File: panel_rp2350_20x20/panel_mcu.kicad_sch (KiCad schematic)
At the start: 32 parts, among them SW1 SW_Push, SW2 SW_Push, U1 APS6404L-3SQR, U2 RP2354B_80QFN, Y1 ABM8-272-T3

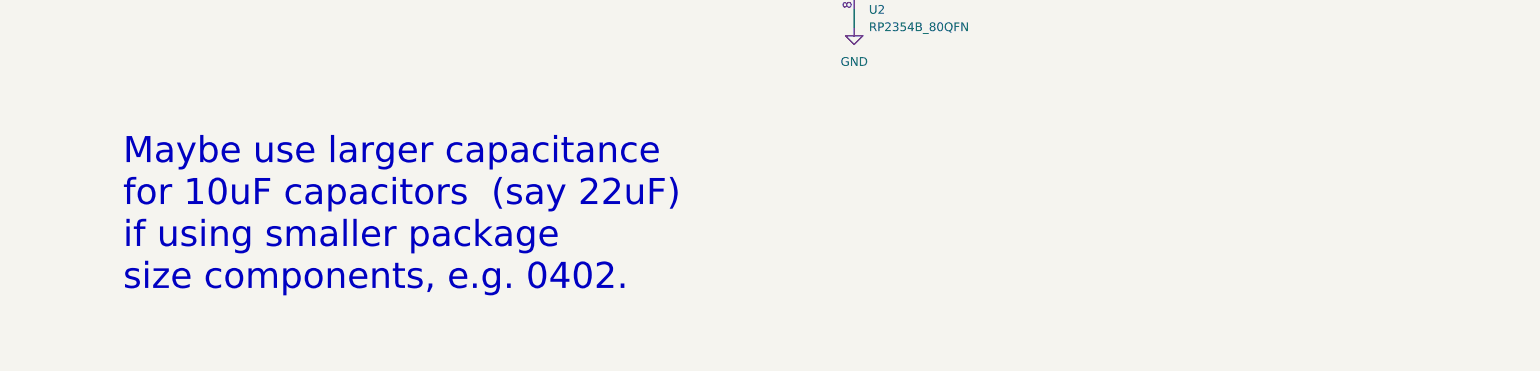
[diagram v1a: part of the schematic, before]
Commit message: Worked on rp2350 20x20 panel layout and routing.
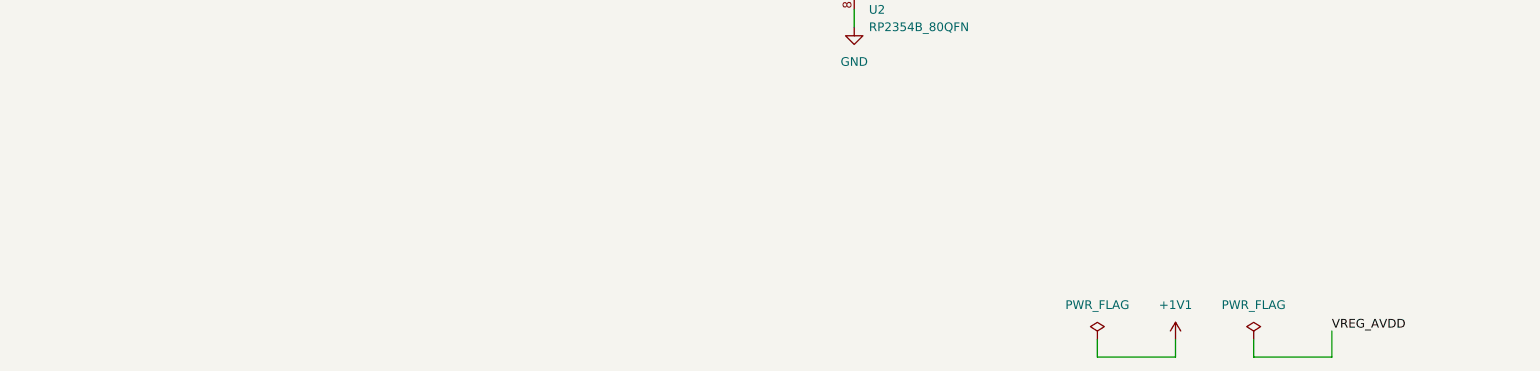
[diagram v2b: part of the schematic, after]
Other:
- note removed: "Maybe use larger capacitance for 10uF capacitors (say 22uF) if using smaller package size components, e.g. 0402."

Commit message: Worked on setup for fabrication.
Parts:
- R6: LCSC Part # (none) -> C295794
- R7, R8: LCSC Part # (none) -> C473051
- SW1, SW2: LCSC Part # (none) -> C720477
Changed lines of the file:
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@@
+			)
+		)
+		(property "LCSC Part #" "C473051"
+			(at 256.54 66.04 0)
+			(effects
+				(font
+					(size 1.27 1.27)
+				)
 			)
 		)
@@
 			)
 		)
+		(property "LCSC Part #" "C720477"
+			(at 63.5 207.01 0)
+			(effects
+				(font
+					(size 1.27 1.27)
+				)
+			)
+		)
 		(pin "1"
 		)
@@
 			)
 		)
+		(property "LCSC Part #" "C295794"
+			(at 148.59 60.96 0)
+			(effects
+				(font
+					(size 1.27 1.27)
+				)
+			)
+		)
 		(pin "1"
 		)
@@
 			)
 		)
+		(property "LCSC Part #" "C720477"
+			(at 44.45 178.435 0)
+			(effects
+				(font
+					(size 1.27 1.27)
+				)
+			)
+		)
 		(pin "1"
 		)
@@
 			(at 256.54 74.93 0)
 			(effects
+				(font
+					(size 1.27 1.27)
+				)
+			)
+		)
+		(property "LCSC Part #" "C473051"
+			(at 256.54 74.93 0)
+			(effects

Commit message: Worked on fab files.
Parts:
- C1, C2: LCSC Part # (none) -> C541259
- C10, C11, C12, C13, C14, C15, C16, C17, C18, C3, C6, C9: LCSC Part # (none) -> C76939
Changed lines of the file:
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@@
+			)
+		)
+		(property "LCSC Part #" "C541259"
+			(at 48.26 116.84 0)
+			(effects
+				(font
+					(size 1.27 1.27)
+				)
+				(hide yes)
 			)
 		)
@@
 			)
 		)
+		(property "LCSC Part #" "C541259"
+			(at 48.26 127 0)
+			(effects
+				(font
+					(size 1.27 1.27)
+				)
+				(hide yes)
+			)
+		)
 		(pin "1"
 		)
@@
 			)
 		)
+		(property "LCSC Part #" "C76939"
+			(at 257.81 36.83 0)
+			(effects
+				(font
+					(size 1.27 1.27)
+				)
+			)
+		)
 		(pin "1"
 		)
@@
 			)
 		)
+		(property "LCSC Part #" "C76939"
+			(at 269.24 36.83 0)
+			(effects
+				(font
+					(size 1.27 1.27)
+				)
+			)
+		)
 		(pin "1"
 		)
@@
 			)
 		)
+		(property "LCSC Part #" "C76939"
+			(at 280.67 36.83 0)
+			(effects
+				(font
+					(size 1.27 1.27)
+				)
+			)
+		)
 		(pin "1"
 		)
@@
 			)
 		)
+		(property "LCSC Part #" "C76939"
+			(at 292.1 36.83 0)
+			(effects
+				(font
+					(size 1.27 1.27)
+				)
+			)
+		)
 		(pin "1"
 		)
@@
 			)
 		)
+		(property "LCSC Part #" "C76939"
+			(at 303.53 36.83 0)
+			(effects
+				(font
+					(size 1.27 1.27)
+				)
+			)
+		)
 		(pin "1"
 		)
@@
 			)
 		)
+		(property "LCSC Part #" "C76939"
+			(at 314.96 36.83 0)
+			(effects
+				(font
+					(size 1.27 1.27)
+				)
+			)
+		)
 		(pin "1"
 		)
@@
 		)
 		(property "Description" ""
+			(at 172.72 36.83 0)
+			(effects
+				(font
+					(size 1.27 1.27)
+				)
+			)
+		)
+		(property "LCSC Part #" "C76939"
 			(at 172.72 36.83 0)
 			(effects
@@
 					(size 1.27 1.27)
 				)
+				(hide yes)
 			)
 		)
@@
 			)
 		)
+		(property "LCSC Part #" "C76939"
+			(at 246.38 36.83 0)
+			(effects
+				(font
+					(size 1.27 1.27)
+				)
+			)
+		)
 		(pin "1"
 		)
@@
 		)
 		(property "Description" ""
+			(at 326.39 36.83 0)
+			(effects
+				(font
+					(size 1.27 1.27)
+				)
+			)
+		)
+		(property "LCSC Part #" "C76939"
 			(at 326.39 36.83 0)
 			(effects
@@
 					(size 1.27 1.27)
 				)
+				(hide yes)
 			)
 		)
@@
 			)
 		)
+		(property "LCSC Part #" "C76939"
+			(at 149.86 36.83 0)
+			(effects
+				(font
+					(size 1.27 1.27)
+				)
+			)
+		)
 		(pin "1"
 		)
@@
 			)
 		)
+		(property "LCSC Part #" "C76939"
+			(at 88.9 76.2 0)
+			(effects
+				(font
+					(size 1.27 1.27)
+				)
+			)
+		)
 		(pin "1"
 		)
@@
 			)
 		)
+		(property "LCSC Part #" "C76939"
+			(at 234.95 36.83 0)
+			(effects
+				(font
+					(size 1.27 1.27)
+				)
+			)
+		)
 		(pin "1"
 		)
@@
 					(size 1.27 1.27)
 				)
+				(hide yes)
 			)
 		)
@@
 					(size 1.27 1.27)
 				)
+				(hide yes)
 			)
 		)
@@
 					(size 1.27 1.27)
 				)
-			)
-		)
+				(hide yes)
+			)
+		)

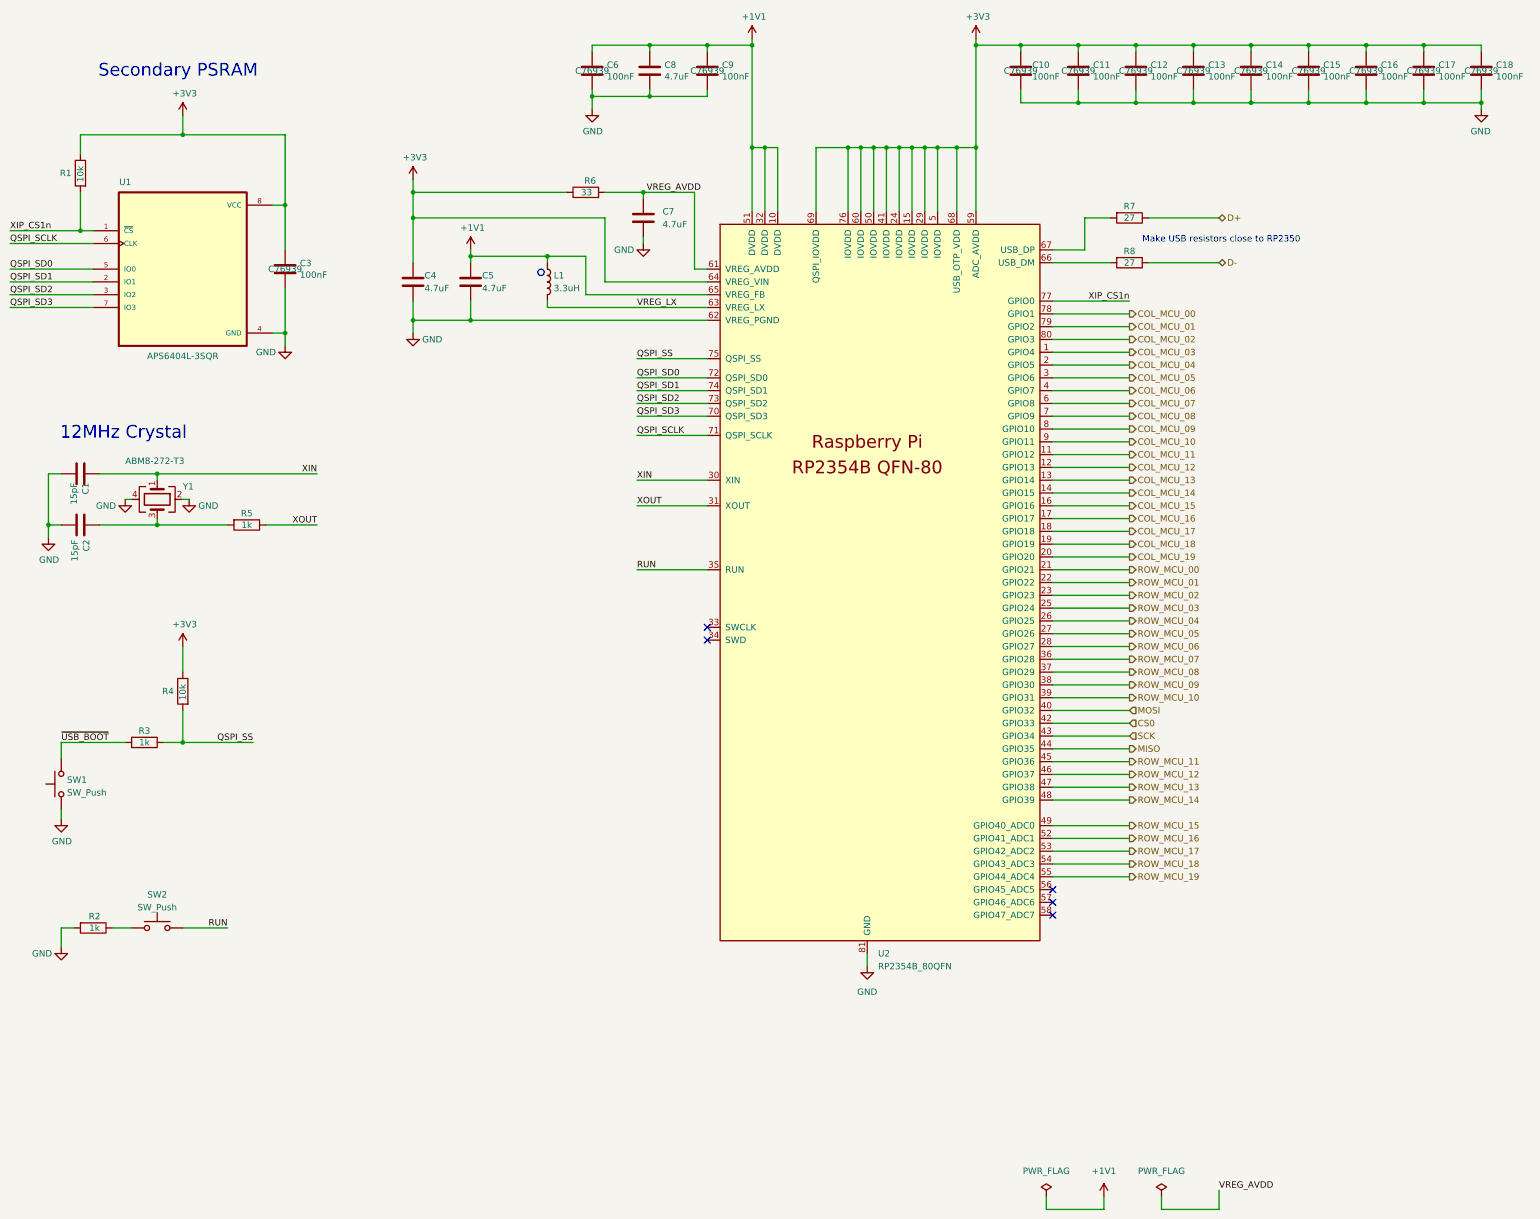
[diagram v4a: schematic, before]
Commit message: Worked on routing and fabrication setup.
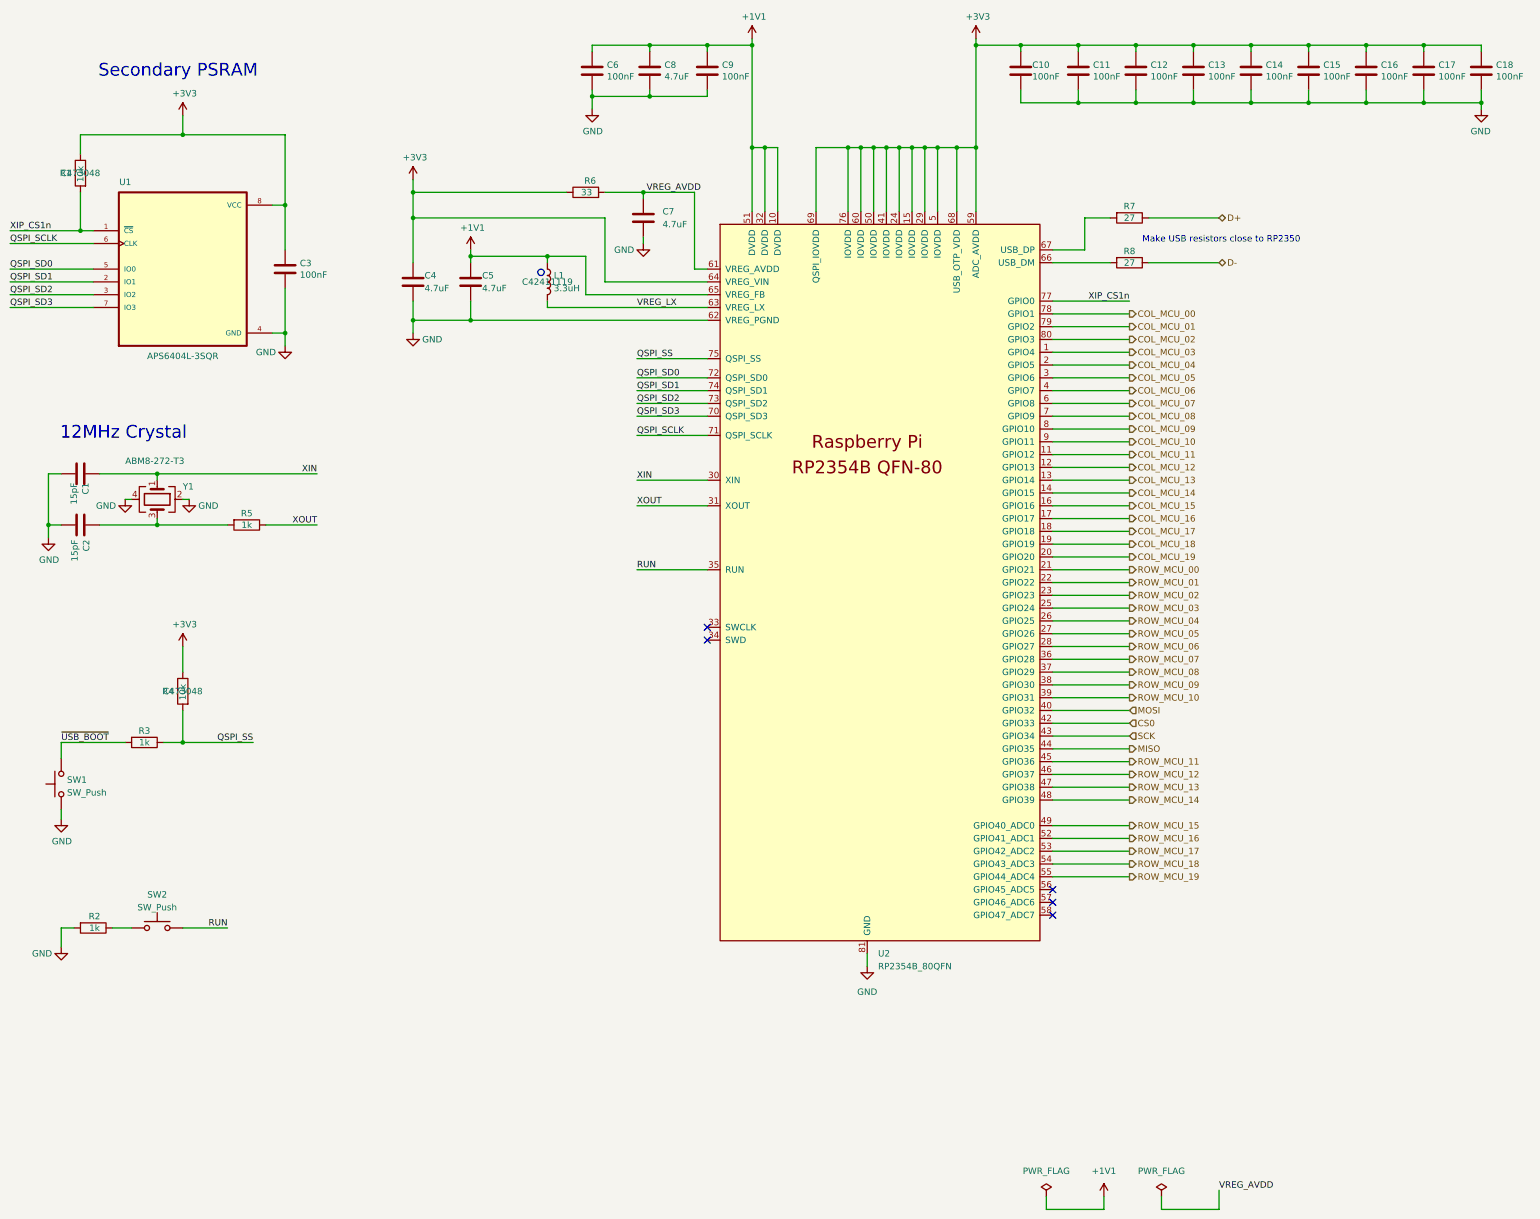
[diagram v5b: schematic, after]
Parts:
- C4, C5, C7, C8: LCSC Part # (none) -> C368809
- L1: LCSC Part # (none) -> C42411119
- R1, R4: LCSC Part # (none) -> C473048
- R2, R3, R5: LCSC Part # (none) -> C270365
- U1: LCSC Part # (none) -> C3040877
- U2: LCSC Part # (none) -> C39843328
- Y1: LCSC Part # (none) -> C20625731
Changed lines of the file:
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@@
 					(size 1.27 1.27)
 				)
+				(hide yes)
 			)
 		)
@@
 					(size 1.27 1.27)
 				)
+				(hide yes)
 			)
 		)
@@
 					(size 1.27 1.27)
 				)
+				(hide yes)
 			)
 		)
@@
 					(size 1.27 1.27)
 				)
+				(hide yes)
 			)
 		)
@@
 					(size 1.27 1.27)
 				)
+				(hide yes)
 			)
 		)
@@
 					(size 1.27 1.27)
 				)
+				(hide yes)
 			)
 		)
@@
 					(size 1.27 1.27)
 				)
+				(hide yes)
 			)
 		)
@@
 					(size 1.27 1.27)
 				)
+				(hide yes)
 			)
 		)
@@
 					(size 1.27 1.27)
 				)
+				(hide yes)
 			)
 		)
@@
 					(size 1.27 1.27)
 				)
+				(hide yes)
 			)
 		)
@@
 					(size 1.27 1.27)
 				)
+				(hide yes)
 			)
 		)
@@
 					(size 1.27 1.27)
 				)
+				(hide yes)
 			)
 		)
@@
 					(size 1.27 1.27)
 				)
+				(hide yes)
 			)
 		)
@@
 					(size 1.27 1.27)
 				)
+				(hide yes)
 			)
 		)
@@
 					(size 1.27 1.27)
 				)
+				(hide yes)
+			)
+		)
+		(property "LCSC Part #" "C20625731"
+			(at 63.5 121.92 0)
+			(effects
+				(font
+					(size 1.27 1.27)
+				)
+				(hide yes)
 			)
 		)
@@
 			)
 		)
+		(property "LCSC Part #" "C3040877"
+			(at 68.58 76.2 0)
+			(effects
+				(font
+					(size 1.27 1.27)
+				)
+				(hide yes)
+			)
+		)
 		(pin "5"
 		)
@@
 					(size 1.27 1.27)
 				)
+				(hide yes)
 			)
 		)
@@
 					(size 1.27 1.27)
 				)
+				(hide yes)
 			)
 		)
@@
 					(size 1.27 1.27)
 				)
+				(hide yes)
 			)
 		)
@@
 					(size 1.27 1.27)
 				)
+				(hide yes)
 			)
 		)
@@
 					(size 1.27 1.27)
 				)
+				(hide yes)
 			)
 		)
@@
 					(size 1.27 1.27)
 				)
+				(hide yes)
 			)
 		)
@@
 					(size 1.27 1.27)
 				)
+				(hide yes)
 			)
 		)
@@
 					(size 1.27 1.27)
 				)
+				(hide yes)
+			)
+		)
+		(property "LCSC Part #" "C473048"
+			(at 68.58 160.02 0)
+			(effects
+				(font
+					(size 1.27 1.27)
+				)
 			)
 		)
@@
 					(size 1.27 1.27)
 				)
+				(hide yes)
+			)
+		)
+		(property "LCSC Part #" "C368809"
+			(at 160.02 66.04 0)
+			(effects
+				(font
+					(size 1.27 1.27)
+				)
+				(hide yes)
 			)
 		)
@@
 			)
 		)
+		(property "LCSC Part #" "C39843328"
+			(at 204.47 115.57 0)
+			(effects
+				(font
+					(size 1.27 1.27)
+				)
+				(hide yes)
+			)
+		)
 		(pin "64"
 		)
@@
 					(size 1.27 1.27)
 				)
+				(hide yes)
+			)
+		)
+		(property "LCSC Part #" "C270365"
+			(at 60.96 170.18 0)
+			(effects
+				(font
+					(size 1.27 1.27)
+				)
+				(hide yes)
 			)
 		)
@@
 			)
 		)
+		(property "LCSC Part #" "C42411119"
+			(at 140.97 78.74 0)
+			(effects
+				(font
+					(size 1.27 1.27)
+				)
+			)
+		)
 		(pin "1"
 		)
@@
 					(size 1.27 1.27)
 				)
+				(hide yes)
+			)
+		)
+		(property "LCSC Part #" "C368809"
+			(at 125.73 78.74 0)
+			(effects
+				(font
+					(size 1.27 1.27)
+				)
+				(hide yes)
 			)
 		)
@@
 					(size 1.27 1.27)
 				)
+				(hide yes)
+			)
+		)
+		(property "LCSC Part #" "C270365"
+			(at 81.28 127 0)
+			(effects
+				(font
+					(size 1.27 1.27)
+				)
+				(hide yes)
 			)
 		)
@@
 					(size 1.27 1.27)
 				)
+				(hide yes)
 			)
 		)
@@
 					(size 1.27 1.27)
 				)
+				(hide yes)
 			)
 		)
@@
 					(size 1.27 1.27)
 				)
+				(hide yes)
 			)
 		)
@@
 					(size 1.27 1.27)
 				)
+				(hide yes)
 			)
 		)
@@
 					(size 1.27 1.27)
 				)
+				(hide yes)
+			)
+		)
+		(property "LCSC Part #" "C368809"
+			(at 161.29 36.83 0)
+			(effects
+				(font
+					(size 1.27 1.27)
+				)
+				(hide yes)
 			)
 		)
@@
 					(size 1.27 1.27)
 				)
+				(hide yes)
 			)
 		)
@@
 					(size 1.27 1.27)
 				)
+				(hide yes)
 			)
 		)
@@
 					(size 1.27 1.27)
 				)
+				(hide yes)
+			)
+		)
+		(property "LCSC Part #" "C270365"
+			(at 50.8 207.01 0)
+			(effects
+				(font
+					(size 1.27 1.27)
+				)
+				(hide yes)
 			)
 		)
@@
 					(size 1.27 1.27)
 				)
+				(hide yes)
 			)
 		)
@@
 					(size 1.27 1.27)
 				)
+				(hide yes)
 			)
 		)
@@
 					(size 1.27 1.27)
 				)
+				(hide yes)
+			)
+		)
+		(property "LCSC Part #" "C368809"
+			(at 114.3 78.74 0)
+			(effects
+				(font
+					(size 1.27 1.27)
+				)
+				(hide yes)
 			)
 		)
@@
 			(at 48.26 57.15 0)
 			(effects
+				(font
+					(size 1.27 1.27)
+				)
+				(hide yes)
+			)
+		)
+		(property "LCSC Part #" "C473048"
+			(at 48.26 57.15 0)
+			(effects

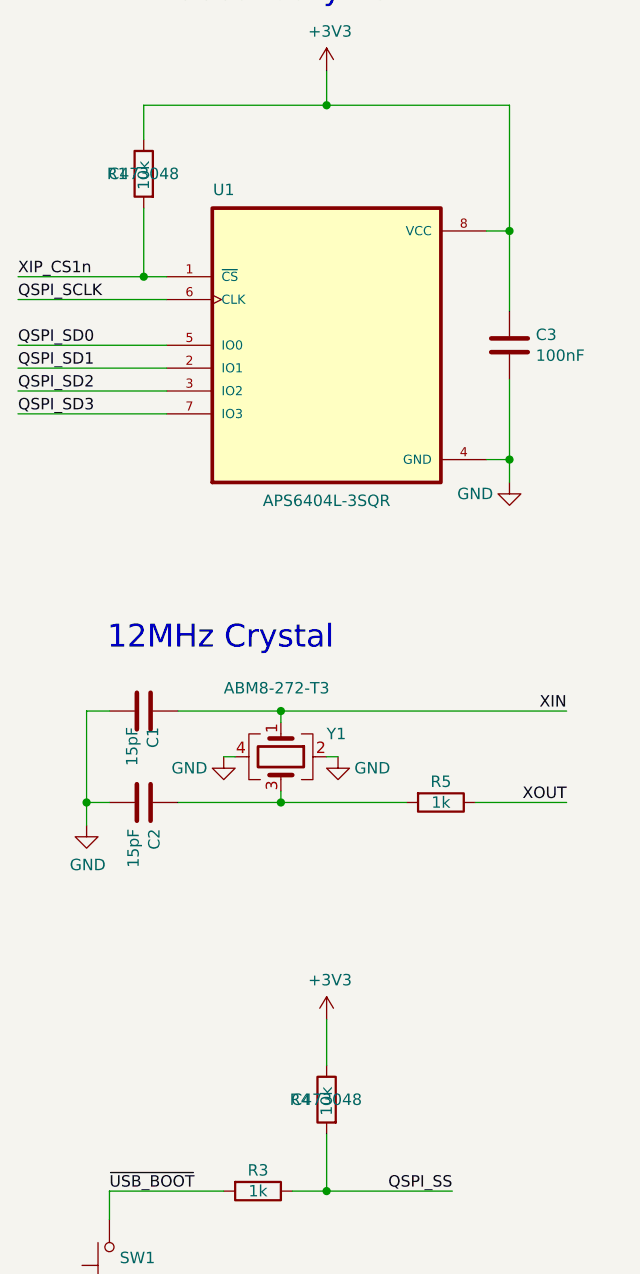
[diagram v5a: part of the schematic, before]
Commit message: Worked on routing, layout and fab setup for rp2354b 20x20 panel.
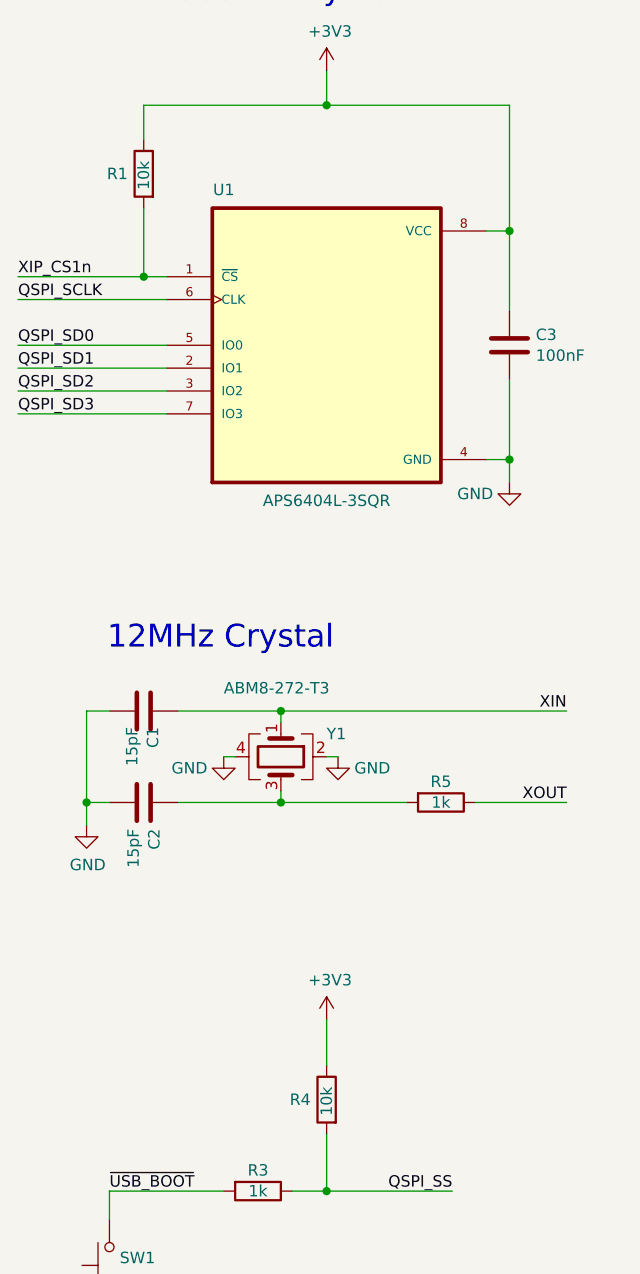
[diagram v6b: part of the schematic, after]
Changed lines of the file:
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@@
 					(size 1.27 1.27)
 				)
+				(hide yes)
 			)
 		)
@@
 					(size 1.27 1.27)
 				)
-			)
-		)
+				(hide yes)
+			)
+		)
